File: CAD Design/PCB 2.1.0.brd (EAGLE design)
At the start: 50 x 40 mm, 51 parts, among them U1 CC2538, U2 MAX1555, X1 32MHz, X2 FC-12M

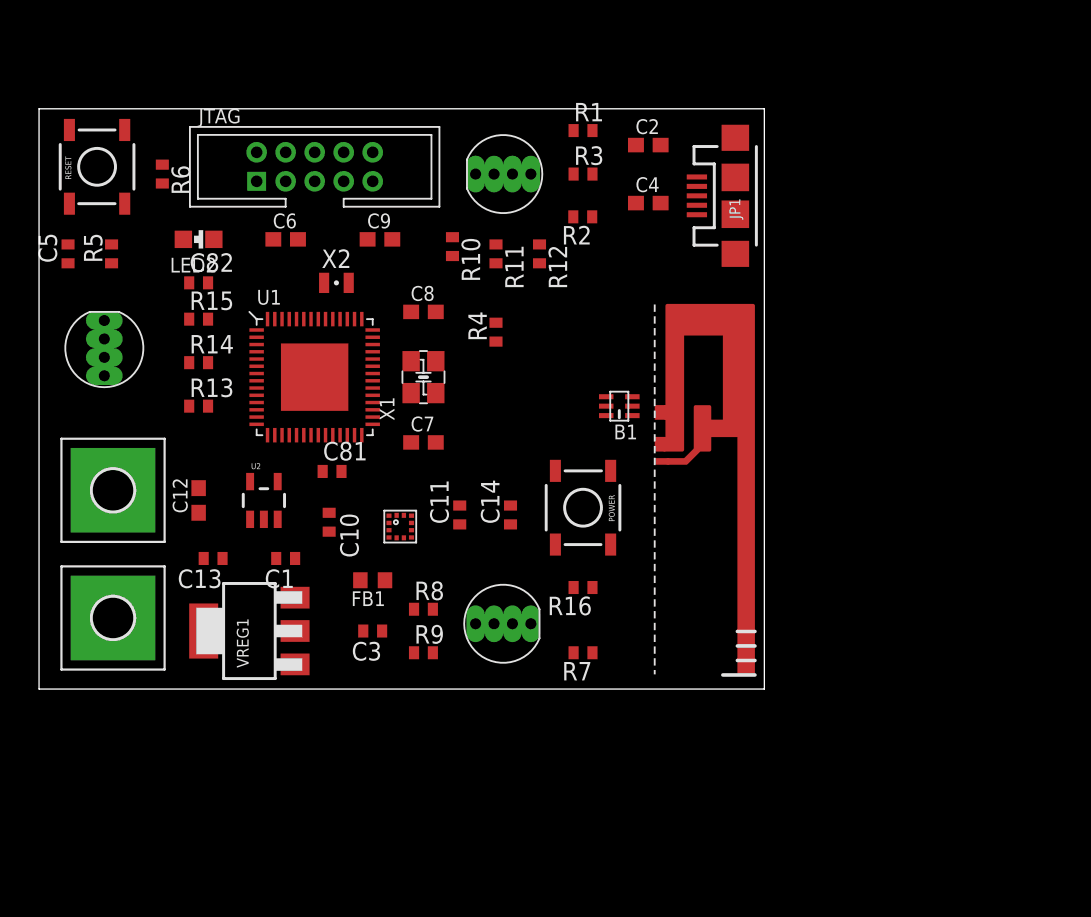
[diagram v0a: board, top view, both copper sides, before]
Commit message: Routing Day Two
Increased board size, rearranged components, ~60% autoroute so far.
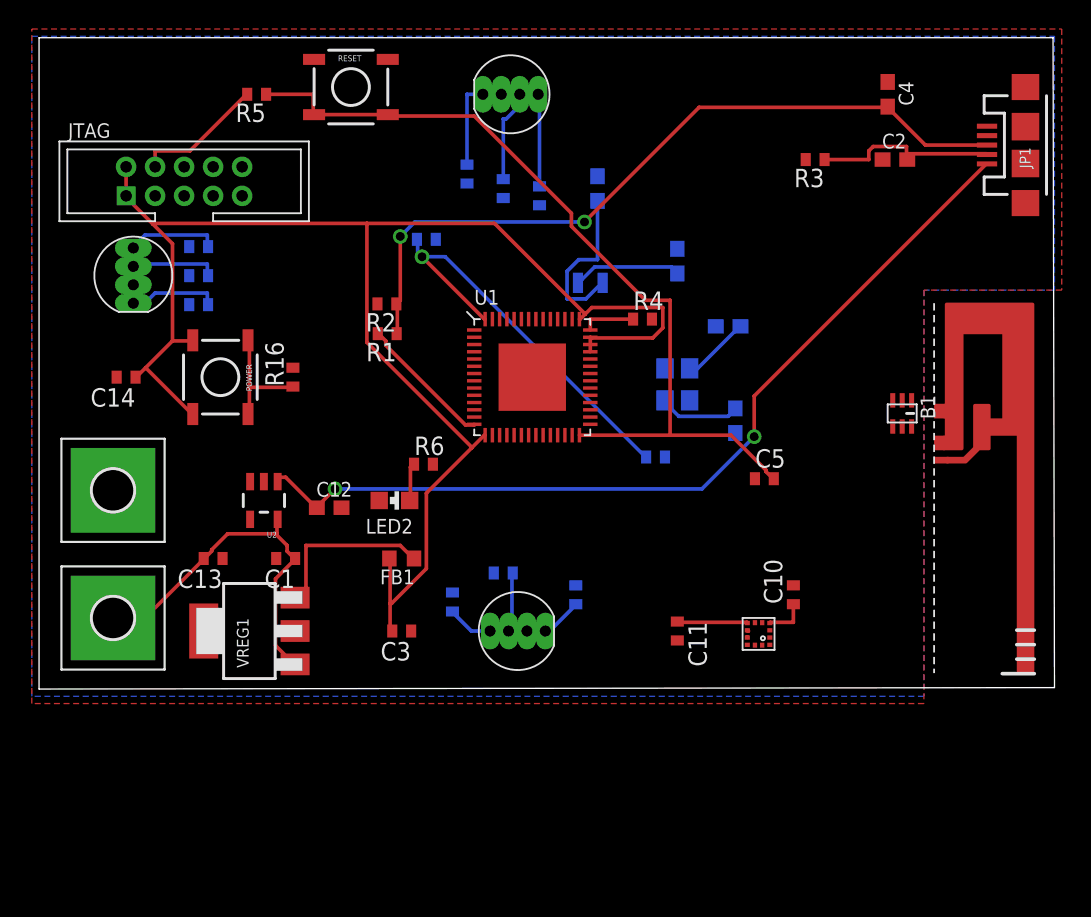
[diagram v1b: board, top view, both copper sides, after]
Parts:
- moved C5 50.4 mm to (50.0, 14.5), turned to 0 degrees
- moved C82 33.7 mm to (42.5, 16.0), flipped to the bottom
- moved C10 32.4 mm to (52.0, 6.50), turned to 90 degrees
- moved C14 28.2 mm to (6.00, 21.5), turned to 180 degrees
- moved R6 26.9 mm to (26.5, 15.5), turned to 0 degrees
- moved POWER 26.6 mm to (12.5, 21.5)
- moved U$1 25.8 mm to (49.6, 3.80), turned to 180 degrees
- moved R16 24.7 mm to (17.5, 21.5), turned to 90 degrees
- moved LED2 22.5 mm to (24.5, 13.0)
- moved C6 21.8 mm to (38.5, 34.5), flipped to the bottom, turned to 270 degrees
- moved C7 21.6 mm to (48.0, 18.5), flipped to the bottom, turned to 90 degrees
- moved C8 21.0 mm to (47.5, 25.0), flipped to the bottom, turned to 180 degrees
- moved C9 20.6 mm to (44.0, 29.5), flipped to the bottom, turned to 270 degrees
- moved JP1 20.3 mm to (68.0, 37.5)
- moved B1 19.5 mm to (59.5, 19.0), turned to 270 degrees
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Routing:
- net 3V3: track 0.00 -> 107.1 mm
- net VBUS: track 0.00 -> 61.5 mm, vias 0 -> 2
- net !RST_PIN: track 0.00 -> 59.1 mm
- net CN1: track 0.00 -> 52.2 mm, vias 0 -> 2
- net DCOUPL: track 0.00 -> 28.8 mm, vias 0 -> 1
- net N$14: track 0.00 -> 25.5 mm
- net N$12: track 0.00 -> 13.2 mm
- net N$17: track 0.00 -> 11.8 mm
- net N$23: track 0.00 -> 11.3 mm
- net N$4: track 0.00 -> 9.49 mm
- net !RST: track 0.00 -> 9.07 mm
- net N$41: track 0.00 -> 8.26 mm
- net N$40: track 0.00 -> 7.52 mm
- net N$29: track 0.00 -> 6.46 mm
- net N$32: track 0.00 -> 6.45 mm
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- added copper zone on layer 1, net GND
- added copper zone on layer 16, net GND
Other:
- board size 50 x 40 mm -> 70 x 44.9 mm

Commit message: End of day 3/9/14
Tried migrating components to bottom, routing attempts failed.
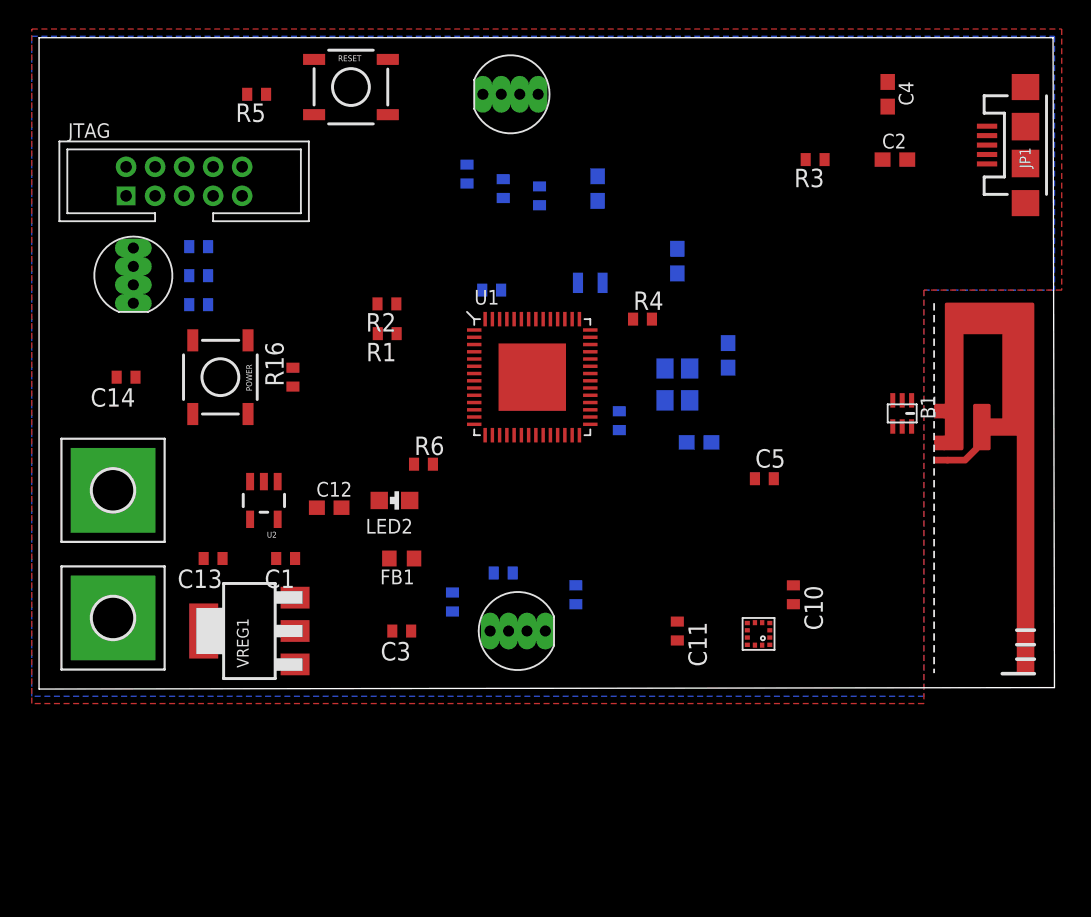
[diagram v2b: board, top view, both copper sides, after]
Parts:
- moved C81 5.70 mm to (31.2, 27.5)
- moved C82 3.54 mm to (40.0, 18.5), turned to 90 degrees
- moved C7 2.92 mm to (45.5, 17.0), turned to 0 degrees
- moved C8 2.00 mm to (47.5, 23.0), turned to 270 degrees
- turned C10 to 270 degrees
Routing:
- net 3V3: track 107.1 -> 0.00 mm
- net VBUS: track 61.5 -> 0.00 mm, vias 2 -> 0
- net !RST_PIN: track 59.1 -> 0.00 mm
- net CN1: track 52.2 -> 0.00 mm, vias 2 -> 0
- net DCOUPL: track 28.8 -> 0.00 mm, vias 1 -> 0
- net N$14: track 25.5 -> 0.00 mm
- net N$12: track 13.2 -> 0.00 mm
- net N$17: track 11.8 -> 0.00 mm
- net N$23: track 11.3 -> 0.00 mm
- net N$4: track 9.49 -> 0.00 mm
- net !RST: track 9.07 -> 0.00 mm
- net N$41: track 8.26 -> 0.00 mm
- net N$40: track 7.52 -> 0.00 mm
- net N$29: track 6.46 -> 0.00 mm
- net N$32: track 6.45 -> 0.00 mm
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
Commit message: 3/16/14 AM fixes
Tweaked schematic as per Jeff’s audit.  Begun re-orienting parts on
board.
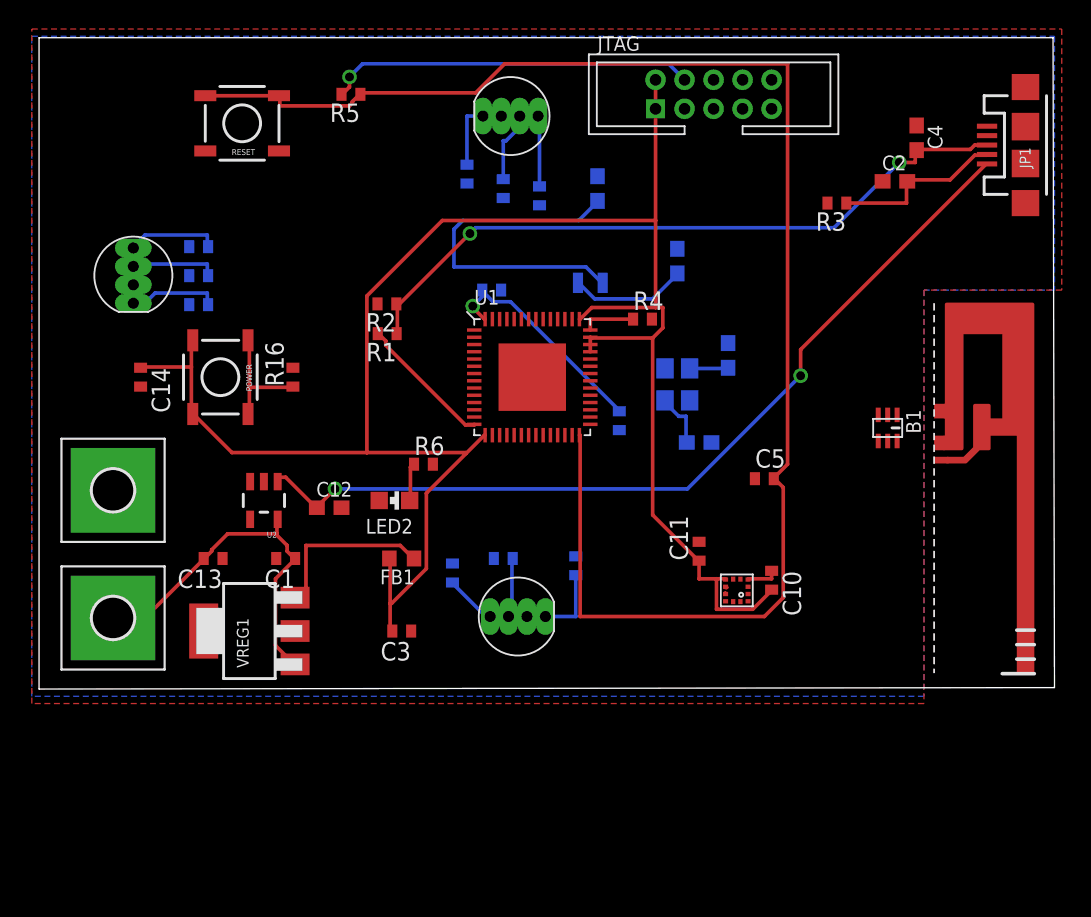
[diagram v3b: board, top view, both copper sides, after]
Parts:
- moved JTAG 37.0 mm to (46.5, 41.0)
- moved RESET 7.91 mm to (14.0, 39.0), turned to 180 degrees
- moved R5 6.50 mm to (21.5, 41.0)
- moved C11 5.70 mm to (45.5, 9.50), turned to 90 degrees
- moved C4 3.61 mm to (60.5, 38.0)
- moved R3 3.35 mm to (55.0, 33.5)
- moved U$1 3.35 mm to (48.1, 6.80)
- moved R7 2.00 mm to (37.0, 8.50)
- moved R9 2.00 mm to (28.5, 8.00)
- moved C10 1.80 mm to (50.5, 7.50)
- moved C2 1.50 mm to (59.0, 35.0)
- moved D4 1.50 mm to (32.5, 39.5)
- moved B1 1.41 mm to (58.5, 18.0)
- moved C14 1.00 mm to (7.00, 21.5), turned to 270 degrees
- moved D1 1.00 mm to (33.0, 5.00)
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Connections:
- removed net RF: B1.1, U$2.GND, U$2.GND@1
- removed net VDD: C11.1, U$1.7
- removed net VDDIO: C10.2, U$1.3
- new net N$45: C10.2, C11.1, U$1.3, U$1.7, U1.30
- net GND: now also U$2.GND, U$2.GND@1; no longer U1.30
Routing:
- net 3V3: track 0.00 -> 127.2 mm
- net !RST_PIN: track 0.00 -> 106.7 mm
- net VBUS: track 0.00 -> 60.9 mm, vias 0 -> 2
- net CN1: track 0.00 -> 47.9 mm, vias 0 -> 2
- net N$14: track 0.00 -> 25.5 mm
- net !RST: track 0.00 -> 25.4 mm, vias 0 -> 1
- net N$23: track 0.00 -> 24.0 mm
- net DCOUPL: track 0.00 -> 15.8 mm, vias 0 -> 1
- net N$12: track 0.00 -> 12.0 mm
- net N$17: track 0.00 -> 11.8 mm
- net N$45: track 0.00 -> 9.54 mm
- net N$4: track 0.00 -> 9.49 mm
- net N$41: track 0.00 -> 8.26 mm
- net N$40: track 0.00 -> 8.06 mm
- net N$25: track 0.00 -> 6.38 mm
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
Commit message: Midday Push
Manual routing ~50% complete.  Needs new accelerometer, yet to
integrate LED driver.
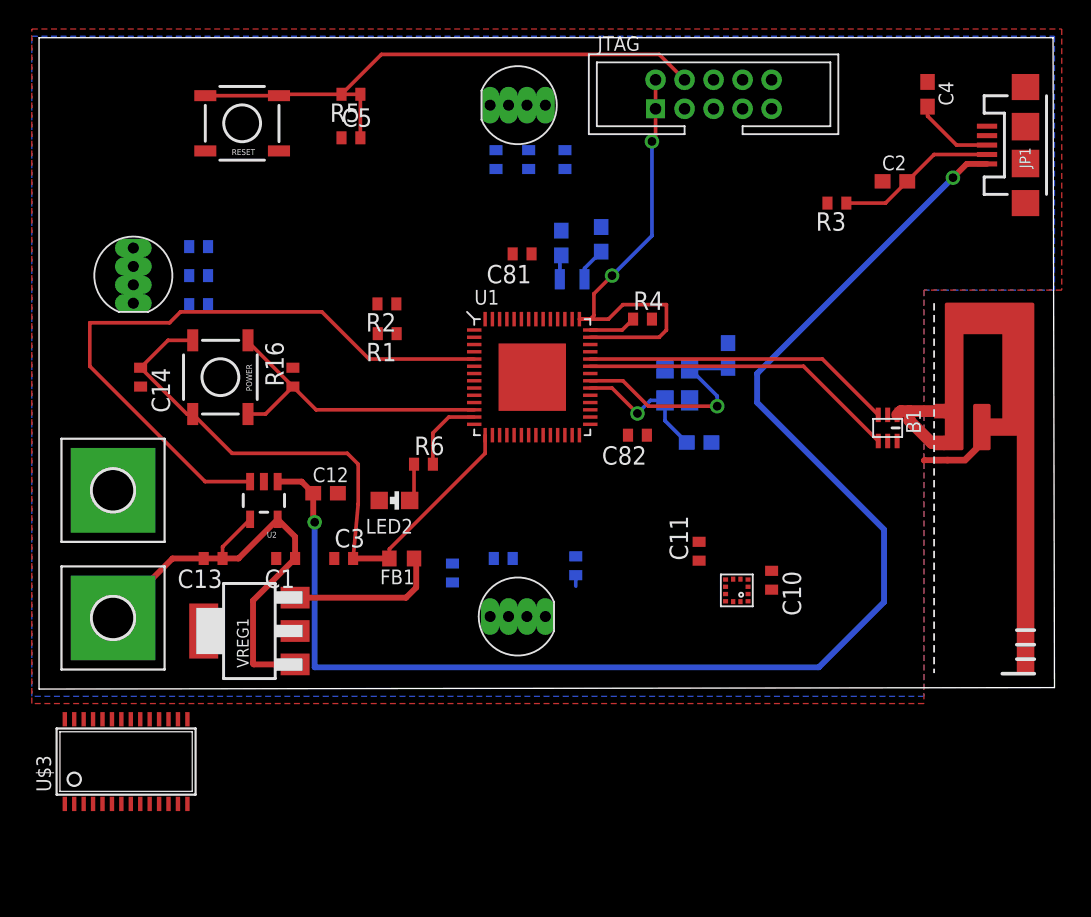
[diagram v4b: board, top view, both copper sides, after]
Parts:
- added U$3: TLC59116, tlc59116:TSSOP28
- moved C5 36.9 mm to (21.5, 38.0)
- moved C3 6.40 mm to (21.0, 9.00), turned to 0 degrees
- moved C9 5.46 mm to (38.8, 31.0)
- moved C6 4.51 mm to (36.0, 30.8)
- moved C81 3.26 mm to (33.3, 30.0), flipped to the top, turned to 180 degrees
- moved C4 3.09 mm to (61.2, 41.0)
- moved R12 3.05 mm to (36.2, 36.5)
- moved R11 2.66 mm to (33.8, 36.5)
- moved R10 2.24 mm to (31.5, 36.5)
- moved C82 1.60 mm to (41.2, 17.5), flipped to the top, turned to 180 degrees
- moved X2 1.27 mm to (36.8, 28.2), turned to 180 degrees
- moved C12 1.03 mm to (19.8, 13.5)
- moved D4 0.90 mm to (33.0, 40.2)
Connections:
- removed net N$19: R10.2, U1.54
- removed net N$20: R11.2, U1.53
- removed net N$22: R12.2, U1.52
- removed net N$33: R15.2, U1.9
- removed net N$34: R14.2, U1.8
- removed net N$36: R13.2, U1.7
- removed net N$37: R9.1, U1.16
- removed net N$38: R8.1, U1.17
- removed net N$39: R7.1, U1.19
- new net RF: B1.1, U$2.GND, U$2.GND@1
- net GND: now also U1.19, U1.52, U1.53, U1.54, U1.7, U1.8, U1.9; no longer U$2.GND, U$2.GND@1
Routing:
- net !RST_PIN: track 106.7 -> 13.7 mm
- net 3V3: track 127.2 -> 75.1 mm, vias 0 -> 2
- net N$21: track 0.00 -> 45.5 mm
- net CN1: track 47.9 -> 5.58 mm, vias 2 -> 0
- net VBUS: track 60.9 -> 97.1 mm
- net N$23: track 24.0 -> 1.69 mm
- net N$28: track 0.00 -> 22.0 mm
- net N$27: track 0.00 -> 21.4 mm
- net DCOUPL: track 15.8 -> 0.00 mm, vias 1 -> 0
- net N$41: track 8.26 -> 21.5 mm
- net N$30: track 2.70 -> 15.5 mm, vias 0 -> 1
- net N$44: track 9.54 -> 0.00 mm
- net N$4: track 9.49 -> 0.00 mm
- net RF: track 0.00 -> 6.39 mm
- net N$25: track 6.38 -> 0.00 mm
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
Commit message: Major Version Update
2.2.0: New accelerometer, LED driver, board ~90% routed
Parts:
- removed C10, C11: 0.1 uF, resistor:C0402
- removed R10, R11, R12, R13, R14, R15: 33, rcl:R0402
- removed U$1: BMA250, DSSCircuits:12LGA_VGG3-D
- added R17: 478, rcl:R0402
- added SW1: (no value), SparkFun-Electromechanical:DIPSWITCH-02
- added U$4: ADXL33X, adafruit:16LCSP
- R7, R8, R9: value 33 -> 1.8k
- moved R7 38.0 mm to (1.00, -3.75), flipped to the top, turned to 0 degrees
- moved U$3 37.7 mm to (17.2, 31.0), turned to 180 degrees
- moved R8 35.6 mm to (1.00, -8.50), flipped to the top, turned to 0 degrees
- moved D3 35.4 mm to (33.0, 5.00), turned to 180 degrees
- moved D1 35.2 mm to (33.0, 40.2)
- moved R9 34.8 mm to (1.00, -13.2), flipped to the top, turned to 0 degrees
- moved D4 32.6 mm to (4.00, 25.2), turned to 90 degrees
- moved C81 4.18 mm to (29.8, 27.8), turned to 270 degrees
- moved C5 2.75 mm to (21.5, 40.8)
- moved C14 1.75 mm to (8.75, 21.5)
- moved R5 1.75 mm to (21.5, 42.8)
- moved RESET 1.75 mm to (14.0, 40.8)
- moved C9 1.50 mm to (37.2, 31.0)
- moved C6 1.00 mm to (35.0, 30.8)
- flipped R1 to the bottom, turned to 0 degrees
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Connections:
- removed net N$3 (its old number): D1.1, R7.2
- removed net N$32: D4.4, R12.1
- removed net N$35: D3.3, R14.1
- removed net N$44: C10.2, C11.1, U$1.3, U$1.7, U1.30
- new net ACCRESET: R9.2, U1.54
- new net ACCSCL: R8.2, U1.52
- new net ACCSDA: R7.2, U1.50
- new net GND3: U$4.3, U$4.5, U$4.6, U$4.7
- new net N$19: R17.1, U$3.1
- new net N$20: D4.4, U$3.17
- new net N$22: D4.3, U$3.16
- new net N$50: R7.1, U$3.27
- new net N$51: R8.1, U$3.26
- new net N$52: R9.1, U$3.25
- net 3V3: now also U$3.28, U$4.14, U$4.15
- net GND: now also R17.2, U$3.2, U$3.3, U$3.4, U$3.5, U1.16, U1.18, U1.26, U1.27, U1.30, U1.31; no longer C10.1, C11.2, U$1.11, U$1.4, U$1.8, U$1.9, U1.19, U1.22, U1.50, U1.52, U1.54
- net N$10: now also U$4.12, U1.19; no longer U$1.1, U1.21
- net N$11: now also C1.1, C13.2, SW1.2, U2.5, VREG1.1; no longer U$1.12, U1.18
- net N$13: now also H1.B2,8, SW1.3; no longer U$1.10, U1.31
- net N$14: now also D1.1, U$3.6; no longer C1.1, C13.2, H1.B2,8, U2.5, VREG1.1
- net N$15: now also D1.3, U$3.7; no longer U$1.2, U1.20
- net N$16: now also U$4.2, U1.22; no longer D1.3, R8.2
- net N$18: now also U$3.8; no longer R9.2
- net N$24: now also U$3.15; no longer R10.1
- net N$25: now also U$3.23; no longer R13.1
- net N$26: now also D3.3, U$3.22; no longer D3.1, R15.1
- net N$29: now also D3.1, U$3.21; no longer D4.3, R11.1
- net N$8: now also U$4.8, U1.21; no longer U$1.5, U1.27
- net N$9: now also U$4.10, U1.20; no longer U$1.6, U1.26
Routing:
- net N$11: track 0.00 -> 61.5 mm, vias 0 -> 2
- net CN1: track 5.58 -> 53.5 mm, vias 0 -> 3
- net !RST_PIN: track 13.7 -> 55.7 mm, vias 0 -> 2
- net N$2: track 0.00 -> 36.4 mm, vias 0 -> 2
- net 3V3: track 75.1 -> 110.4 mm
- net N$13: track 0.00 -> 30.9 mm, vias 0 -> 2
- net PB6: track 0.00 -> 27.9 mm
- net N$6: track 0.00 -> 23.3 mm
- net PB7: track 0.00 -> 21.6 mm
- net N$7: track 0.00 -> 20.3 mm
- net N$15: track 0.00 -> 18.8 mm
- net N$18: track 0.25 -> 18.5 mm
- net GND: track 4.70 -> 17.9 mm, vias 0 -> 1
- net N$4: track 0.00 -> 10.4 mm, vias 0 -> 1
- net N$14: track 28.7 -> 19.6 mm
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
